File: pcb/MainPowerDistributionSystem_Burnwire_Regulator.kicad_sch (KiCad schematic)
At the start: 12 parts, among them U7 L4978

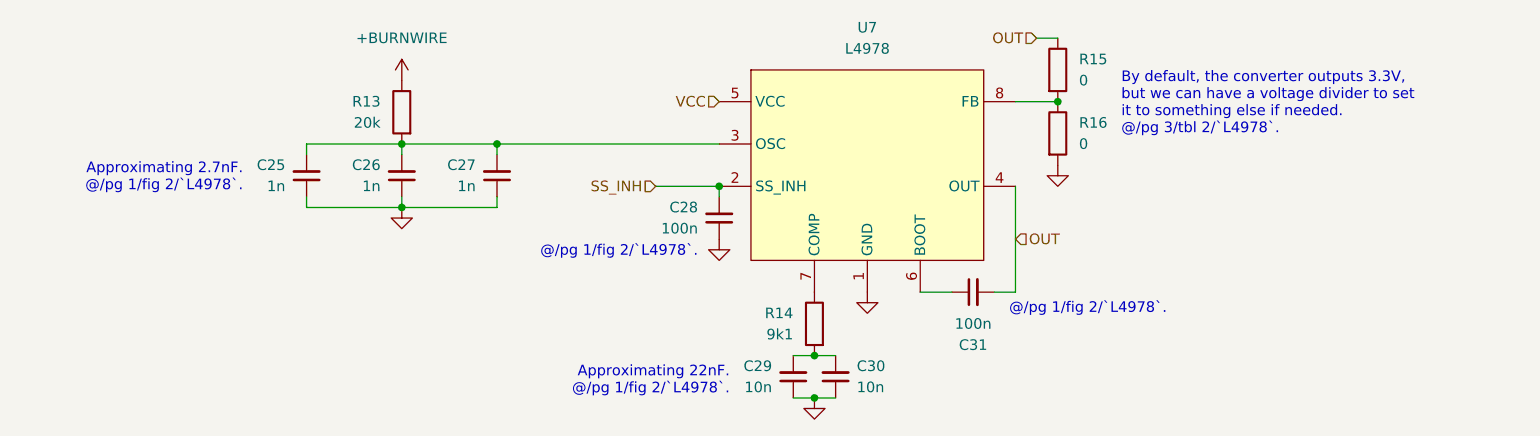
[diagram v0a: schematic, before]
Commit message: Fixed issues reported by `checkPCBs` concerning the stack connectors.
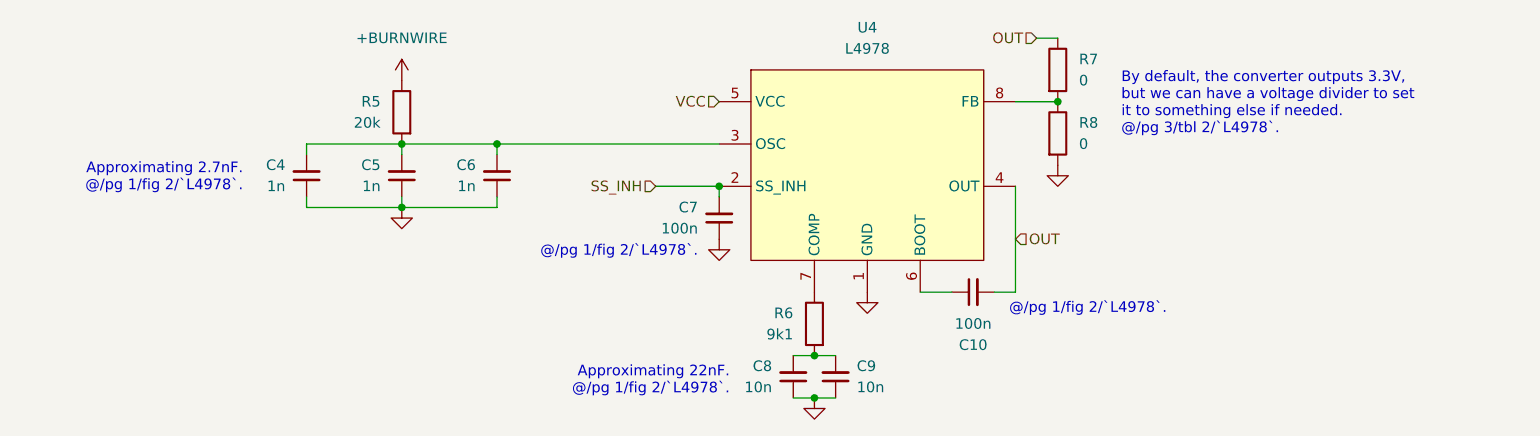
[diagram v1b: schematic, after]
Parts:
- renumbered C31 to C10, C25 to C4, C26 to C5, C27 to C6, C28 to C7, C29 to C8, C30 to C9, R13 to R5, R14 to R6, R15 to R7, R16 to R8, U7 to U4
